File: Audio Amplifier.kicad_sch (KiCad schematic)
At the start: 40 parts, among them J1 AudioJack3, J2 +12V 5A regulated power supply, SW1 SW_SPST, U1 TPA3110D2PWP

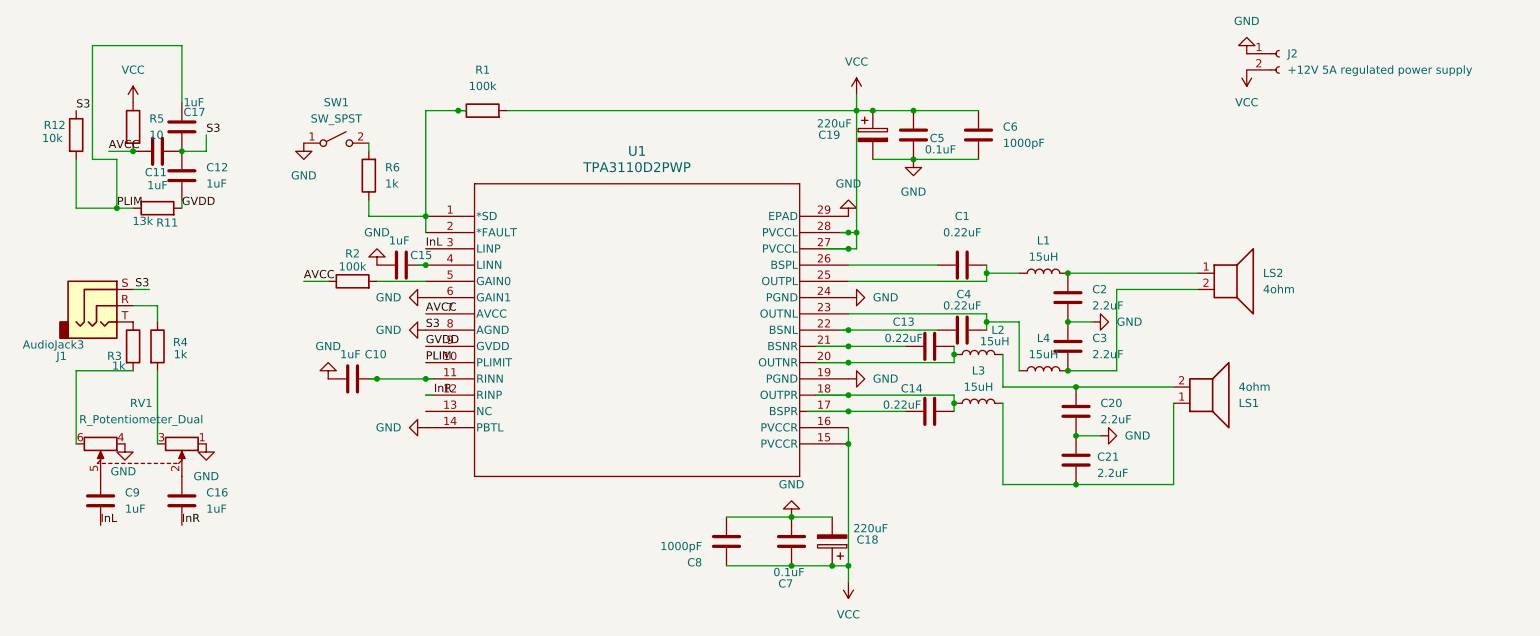
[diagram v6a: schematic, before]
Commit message: Fix(General): Added values to a few components that were missing them.
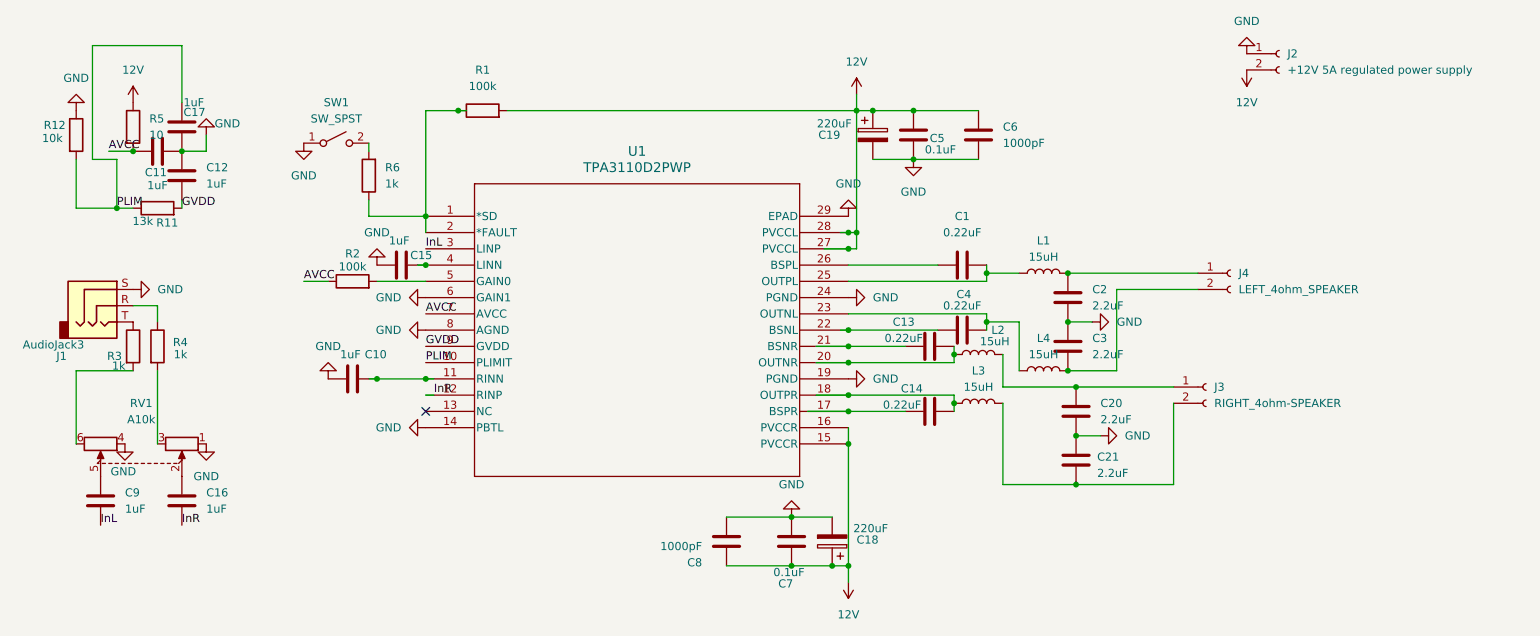
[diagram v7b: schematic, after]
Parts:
- removed LS1, LS2: 4ohm, symbol Device:Speaker
- added J3: RIGHT_4ohm-SPEAKER, symbol Connector:Conn_01x02_Socket
- added J4: LEFT_4ohm_SPEAKER, symbol Connector:Conn_01x02_Socket
- RV1: value R_Potentiometer_Dual -> A10k
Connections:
- net at C2.1, L1.2: now also J4.1 (Pin_1)
- net at C20.1, L2.2: now also J3.1 (Pin_1)
- net at C21.2, L3.2: now also J3.2 (Pin_2)
- net at C3.2, L4.2: now also J4.2 (Pin_2)
- net VCC renamed 12V
- no-connect marks 0 -> 1

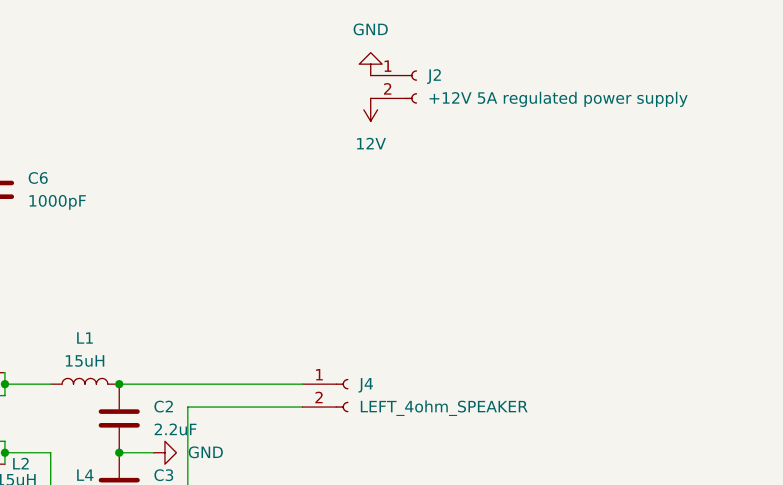
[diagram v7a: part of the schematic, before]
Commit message: Feat(VCC): Added input protection around the power connector using pmos and a zener diode. Changed the VCC label to +12V for clarity.
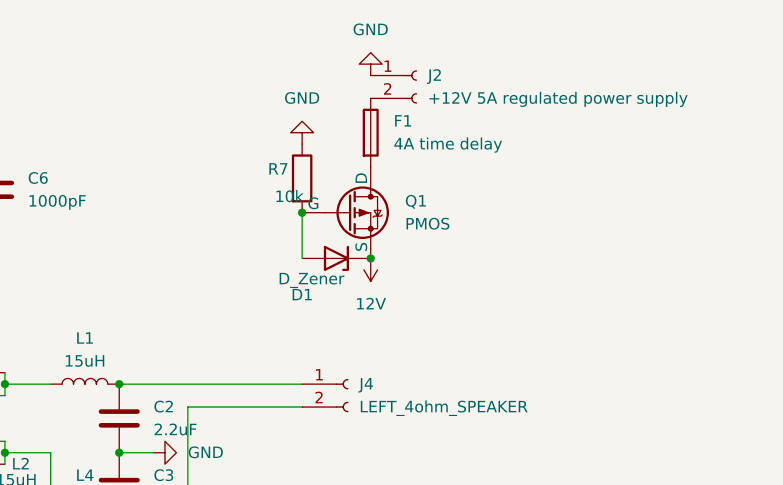
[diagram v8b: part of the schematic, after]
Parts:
- added D1: D_Zener, symbol Device:D_Zener
- added F1: 4A time delay, symbol Device:Fuse
- added Q1: PMOS, symbol Simulation_SPICE:PMOS
- added R7: 10k, symbol Device:R
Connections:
- net 12V: now also D1.1 (K), Q1.3 (S); no longer J2.2 (Pin_2)
- net GND: now also R7.1
- new net: F1.1, J2.2 (Pin_2)
- new net: F1.2, Q1.1 (D)
- new net: D1.2 (A), Q1.2 (G), R7.2
